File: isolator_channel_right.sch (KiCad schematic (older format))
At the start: 44 parts, among them U301 NE5532, U302 NE5532, U303 NE5532, U304 NE5532, U305 NE5532, U306 NE5532, U307 NE5532, U308 NE5532

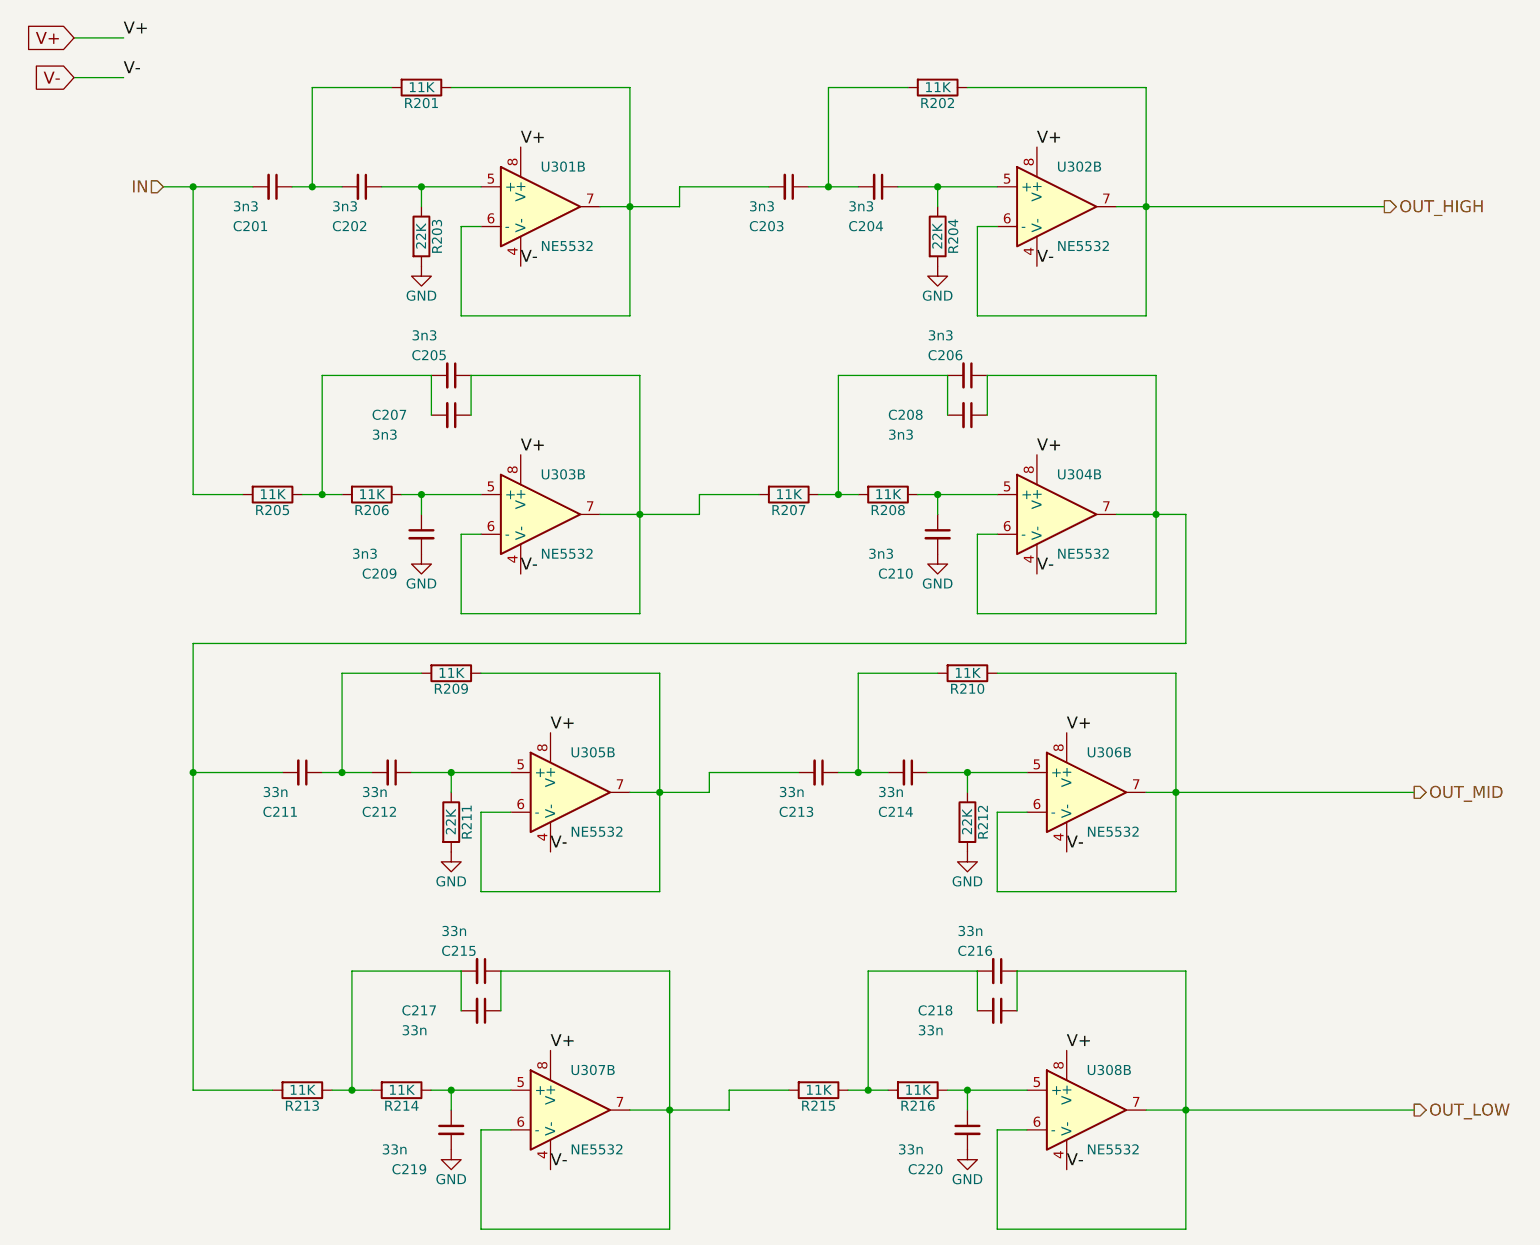
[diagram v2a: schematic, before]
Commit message: Updated components references and properties
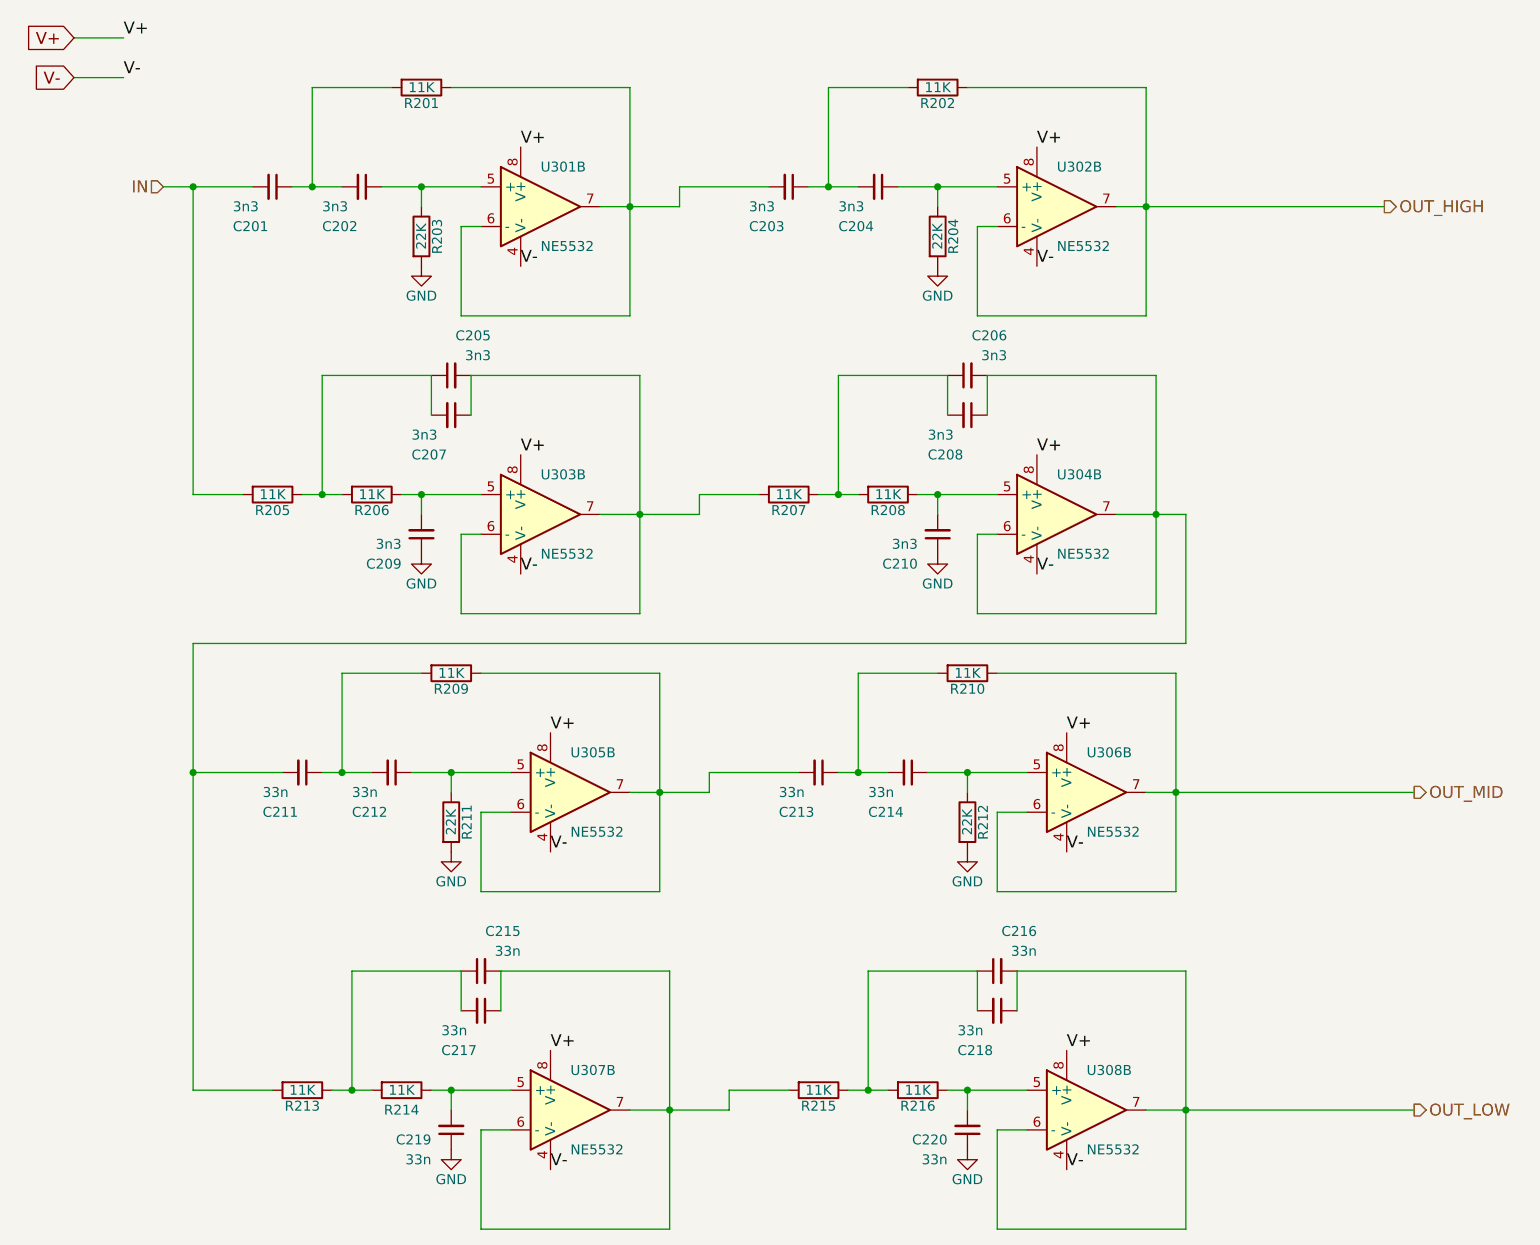
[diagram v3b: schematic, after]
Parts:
- C201, C202, C203, C204, C205, C206, C207, C208, C209, C210: footprint Capacitors_THT:C_Rect_L7.0mm_W3.5mm_P5.00mm -> Capacitors_THT:C_Rect_L7.0mm_W2.5mm_P5.00mm; Description (none) -> Condensateurs à film 100volts 3300pF 5%; Distributor (none) -> Mouser; Distributor Part # (none) -> 80-R82EC1330JE50J; Manufacturer (none) -> Kemet; Mfg_Part_# (none) -> R82EC1330JE50J; Package (none) -> 2-THT
- C211, C212, C213, C214, C215, C216, C217, C218, C219, C220: Description (none) -> Condensateurs à film 100volts .033uF 5%; Distributor (none) -> Mouser; Distributor Part # (none) -> 80-R82EC2330AA50J; Manufacturer (none) -> Kemet; Mfg_Part_# (none) -> R82EC2330AA50J; Mfg_Part_No QYX1H333KTP -> R82EC2330AA50J; Package (none) -> 2-THT
- R201, R202, R205, R206, R207, R208, R209, R210, R213, R214, R215, R216: Description (none) -> Résistances à couche métallique - Trou traversant 1/3watts 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; Distributor (none) -> Mouser; Distributor Part # (none) -> 71-CCF50-11K; Manufacturer (none) -> Vishay / Dale; Mfg_Part_# (none) -> CCF5011K0FKR36; Package (none) -> DIN0204
- R203, R204, R211, R212: Description (none) -> Résistances à couche métallique - Trou traversant 1/3watts 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; Distributor (none) -> Mouser; Distributor Part # (none) -> 71-CCF50-J-22K; Manufacturer (none) -> Vishay / Dale; Mfg_Part_# (none) -> CCF5022K0JKR36; Package (none) -> DIN0204
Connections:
- net GND: now also C209.1, C210.1, C219.1, C220.1; no longer C209.2, C210.2, C219.2, C220.2
- net OUT_LOW: now also C216.2; no longer C216.1
- net at C207.1, R207.2, U303.6 (-)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: now also C205.2; no longer C205.1
- net at C207.2, R205.1, R206.2: now also C205.1; no longer C205.2
- net at C208.1, C211.2, R213.2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: now also C206.2; no longer C206.1
- net at C208.2, R207.1, R208.2: now also C206.1; no longer C206.2
- net at R214.1, U307.5 (+): now also C219.2; no longer C219.1
- net at C217.2, R213.1, R214.2: now also C215.1; no longer C215.2
- net at R216.1, U308.5 (+): now also C220.2; no longer C220.1
- net at C218.2, R215.1, R216.2: now also C216.1; no longer C216.2
- net at R206.1, U303.5 (+): now also C209.2; no longer C209.1
- net at R208.1, U304.5 (+): now also C210.2; no longer C210.1
- net at C217.1, R215.2, U307.6 (-)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: now also C215.2; no longer C215.1
